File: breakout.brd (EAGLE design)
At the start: 55.9 x 12.7 mm, 8 parts, among them P1@1 M01PTH, P1@2 M01PTH, P2@1 M01PTH, P2@2 M01PTH, P3@1 M01PTH, P3@2 M01PTH

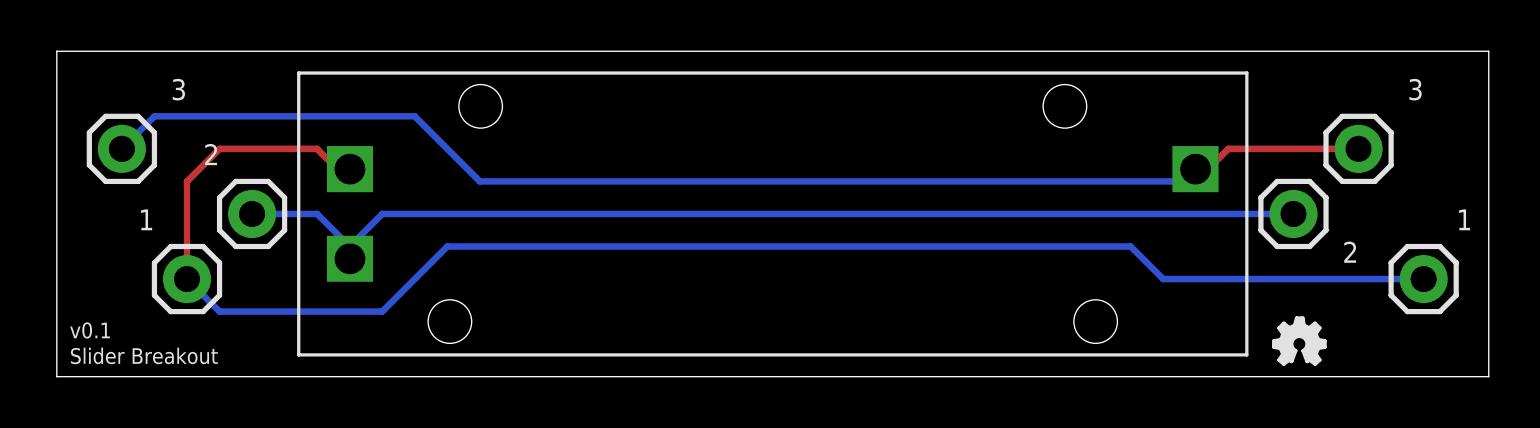
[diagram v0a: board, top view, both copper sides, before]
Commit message: increasing font and oshw logo size
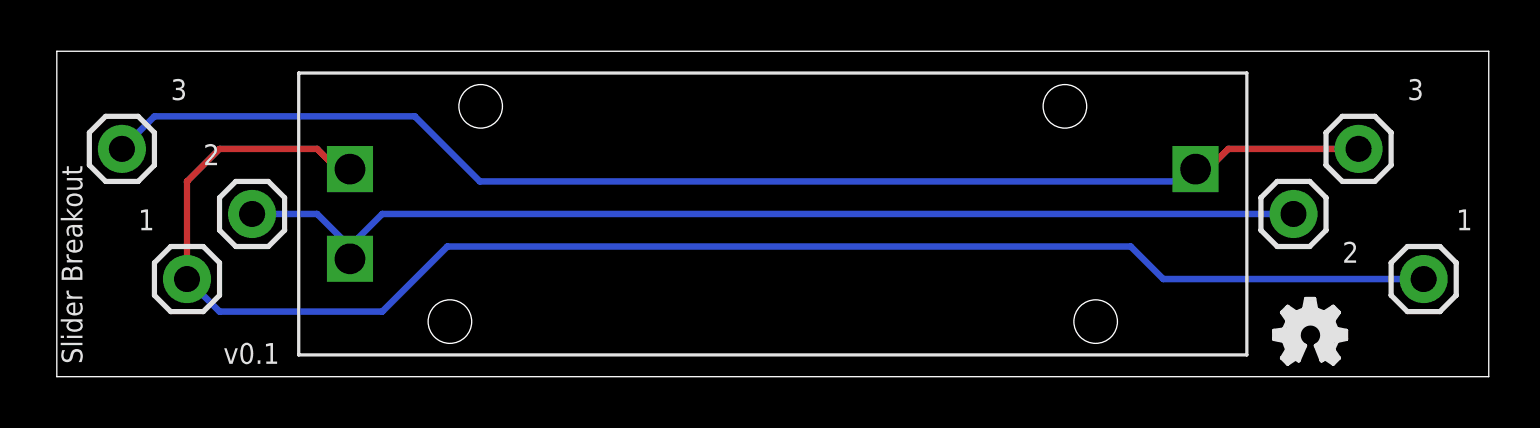
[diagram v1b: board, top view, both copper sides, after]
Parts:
- LOGO1: value OSHW_LOGO_FILLX0070-NT -> OSHW_LOGO_FILLX0100-NT; device ohw-logo:OSHW_FILLX70_NOTEXT -> ohw-logo:OSHW_FILLX100_NOTEXT
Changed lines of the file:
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@@
 <setting verticaltext="up"/>
 </settings>
-<grid distance="0.5" unitdist="mm" unit="mm" style="lines" multiple="1" display="yes" altdistance="0.5" altunitdist="inch" altunit="inch"/>
+<grid distance="50" unitdist="mil" unit="mil" style="lines" multiple="1" display="yes" altdistance="0.5" altunitdist="inch" altunit="inch"/>
 <layers>
 <layer number="1" name="Top" color="4" fill="1" visible="yes" active="yes"/>
@@
 <text x="50.165" y="4.445" size="0.8128" layer="21">2</text>
 <text x="54.61" y="5.715" size="0.8128" layer="21">1</text>
-<text x="0.5" y="1.5" size="0.6096" layer="21">v0.1</text>
-<text x="0.5" y="0.5" size="0.6096" layer="21">Slider Breakout</text>
+<text x="6.5" y="0.5" size="0.8128" layer="21">v0.1</text>
+<text x="1" y="0.5" size="0.8128" layer="21" rot="R90">Slider Breakout</text>
 </plain>
 <attributes>
@@
 <element name="P2@2" library="SparkFun-Connectors" package="1X01" value="M01PTH" x="48.26" y="6.35" smashed="yes"/>
 <element name="P1@2" library="SparkFun-Connectors" package="1X01" value="M01PTH" x="53.34" y="3.81" smashed="yes"/>
-<element name="LOGO1" library="ohw-logo" package="OSHW_FILLX70_NOTEXT" value="OSHW_LOGO_FILLX0070-NT" x="47.5" y="0.5"/>
+<element name="LOGO1" library="ohw-logo" package="OSHW_FILLX100_NOTEXT" value="OSHW_LOGO_FILLX0100-NT" x="47.5" y="0.5"/>
 </elements>
 <signals>
